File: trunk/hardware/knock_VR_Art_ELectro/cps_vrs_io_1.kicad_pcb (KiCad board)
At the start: 2 copper layers, 31.1 x 20.3 mm, 35 parts, among them P1 CONN_1, P2 CONN_1, P3 CONN_5X2, P4 CONN_4, U20 MAX9926/9927, U24 MAX9939

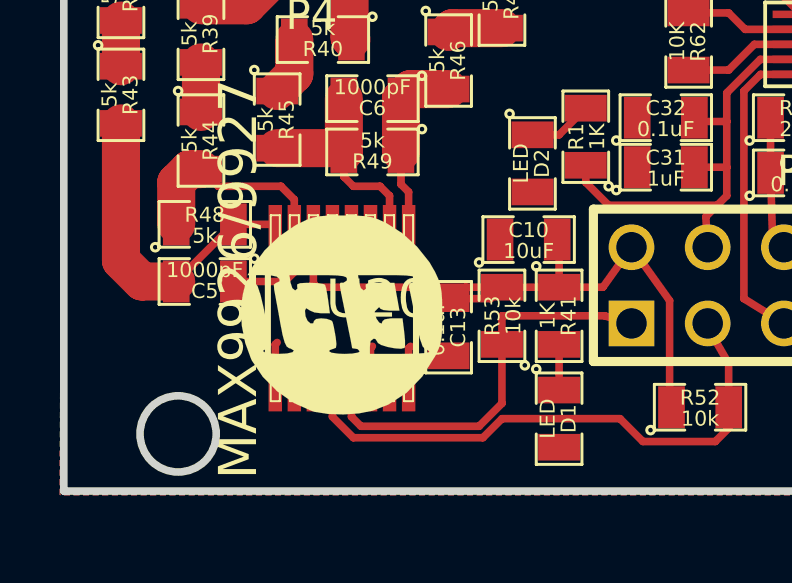
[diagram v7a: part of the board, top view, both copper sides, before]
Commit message: logo on the correct side
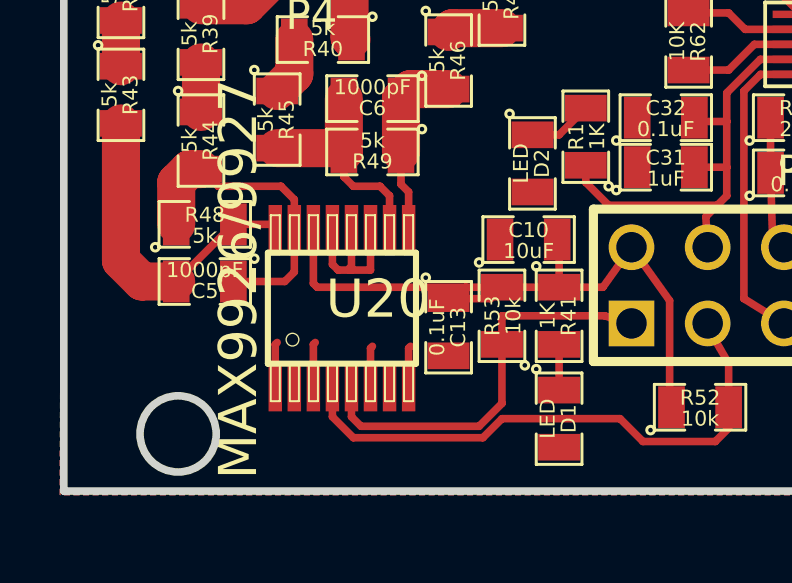
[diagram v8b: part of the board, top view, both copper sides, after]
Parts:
- G1: moved to B.Cu
- moved G1 0.85 mm to (219.7, 67.3)
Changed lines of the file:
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@@
-(kicad_pcb (version 3) (host pcbnew "(2013-mar-13)-testing")
+(kicad_pcb (version 3) (host pcbnew "(2013-07-07 BZR 4022)-stable")
   (general
     (links 67)
@@
   (page A4)
   (title_block
-    (date "03 Dec 2013")
     (company Art_Electro)
     (comment 1 cps_vrs_io_1)
@@
   )
   (setup
-    (last_trace_width 1.27)
+    (last_trace_width 0.254)
     (user_trace_width 0.5)
     (user_trace_width 1.27)
@@
     )
   )
-  (module LOGO_F (layer F.Cu)
-    (at 220.091 66.548)
-    (fp_text reference G1 (at 0 4.14782) (layer F.SilkS) hide
-      (effects (font (thickness 0.3048)))
-    )
-    (fp_text value LOGO (at 0 -4.14782) (layer F.SilkS) hide
-      (effects (font (thickness 0.3048)))
+  (module LOGO_F (layer B.Cu)
+    (at 219.71 67.31)
+    (fp_text reference G1 (at 0 -4.14782) (layer B.SilkS) hide
+      (effects (font (size 1.524 1.524) (thickness 0.3048)) (justify mirror))
+    )
+    (fp_text value LOGO (at 0 4.14782) (layer B.SilkS) hide
+      (effects (font (size 1.524 1.524) (thickness 0.3048)) (justify mirror))
     )
     (fp_poly (pts (xy 3.34518 -0.04318) (xy 3.3401 0.381) (xy 3.32486 0.68326) (xy 3.28676 0.90932)
@@
       (xy 1.47574 -3.09372) (xy 2.00914 -2.7559) (xy 2.50444 -2.30378) (xy 2.91592 -1.78816)
       (xy 3.10134 -1.46812) (xy 3.21056 -1.2319) (xy 3.28168 -1.02616) (xy 3.31978 -0.8001)
-      (xy 3.3401 -0.50546) (xy 3.34264 -0.09398) (xy 3.34518 -0.04318) (xy 3.34518 -0.04318)) (layer F.SilkS) (width 0.00254))
+      (xy 3.3401 -0.50546) (xy 3.34264 -0.09398) (xy 3.34518 -0.04318) (xy 3.34518 -0.04318)) (layer B.SilkS) (width 0.00254))
   )
   (dimension 31.115 (width 0.381) (layer Cmts.User)
@@
   (segment (start 241.046 56.97624) (end 241.046 54.356) (width 0.254) (layer F.Cu) (net 15))
   (segment (start 241.02262 56.99962) (end 241.046 56.97624) (width 0.254) (layer F.Cu) (net 15))
-  (segment (start 239.60058 57.5) (end 238.475 57.5) (width 0.254) (layer F.Cu) (net 16) (status 10))
-  (segment (start 238.475 57.5) (end 238.125 57.15) (width 0.254) (layer F.Cu) (net 16))
   (segment (start 222.3135 68.98386) (end 222.3135 67.6275) (width 0.254) (layer F.Cu) (net 16) (status 10))
   (segment (start 222.3135 67.6275) (end 222.377 67.564) (width 0.254) (layer F.Cu) (net 16))
@@
   (segment (start 219.964 65.024) (end 220.345 65.024) (width 0.254) (layer F.Cu) (net 16))
   (segment (start 219.7735 64.8335) (end 219.964 65.024) (width 0.254) (layer F.Cu) (net 16))
+  (segment (start 239.60058 57.5) (end 238.475 57.5) (width 0.254) (layer F.Cu) (net 16) (status 10))
+  (segment (start 238.475 57.5) (end 238.125 57.15) (width 0.254) (layer F.Cu) (net 16))
   (segment (start 234.3785 54.2925) (end 234.3785 55.47832) (width 0.254) (layer F.Cu) (net 17) (status 10))
   (segment (start 234.3785 55.47832) (end 235.39942 56.49924) (width 0.254) (layer F.Cu) (net 17) (status 20))
@@
   (segment (start 214.5665 62.103) (end 214.5665 63.5) (width 1.27) (layer F.Cu) (net 27))
   (segment (start 215.011 61.6585) (end 214.5665 62.103) (width 1.27) (layer F.Cu) (net 27))
-  (segment (start 218.5035 63.60414) (end 218.5035 62.6745) (width 0.254) (layer F.Cu) (net 27))
+  (segment (start 218.5035 63.60414) (end 218.5035 62.6745) (width 0.254) (layer F.Cu) (net 27) (status 10))
   (segment (start 215.9635 62.23) (end 215.392 61.6585) (width 0.254) (layer F.Cu) (net 27))
   (segment (start 218.059 62.23) (end 215.9635 62.23) (width 0.254) (layer F.Cu) (net 27))
@@
   (segment (start 213.4235 65.405) (end 212.725 64.7065) (width 1.27) (layer F.Cu) (net 28))
   (segment (start 216.4715 63.5) (end 214.5665 65.405) (width 0.254) (layer F.Cu) (net 28) (status 30))
-  (segment (start 216.4715 63.5) (end 217.76436 63.5) (width 0.254) (layer F.Cu) (net 28) (status 30))
+  (segment (start 216.4715 63.5) (end 217.76436 63.5) (width 0.254) (layer F.Cu) (net 28) (status 20))
   (segment (start 217.76436 63.5) (end 217.8685 63.60414) (width 0.254) (layer F.Cu) (net 28) (status 30))
   (segment (start 235.39942 57.5) (end 236.6335 57.5) (width 0.254) (layer F.Cu) (net 29) (status 10))
